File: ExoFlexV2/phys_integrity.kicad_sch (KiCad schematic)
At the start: 23 parts

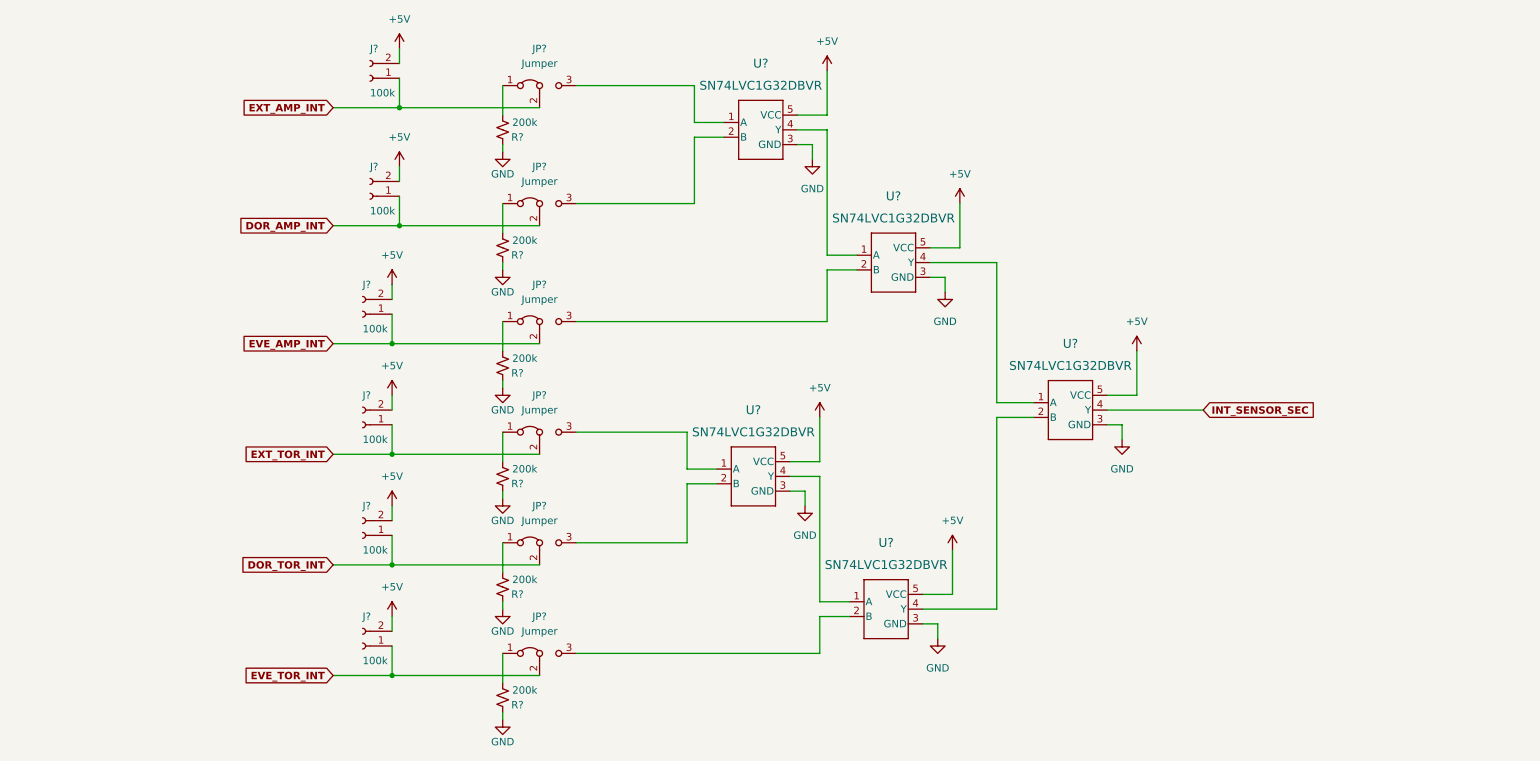
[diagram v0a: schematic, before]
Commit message: Mise à jour signaux STM
- Condo de découplage
- Signaux supplémentaire pour le STM
- Page GND sera pour Multiplexeur
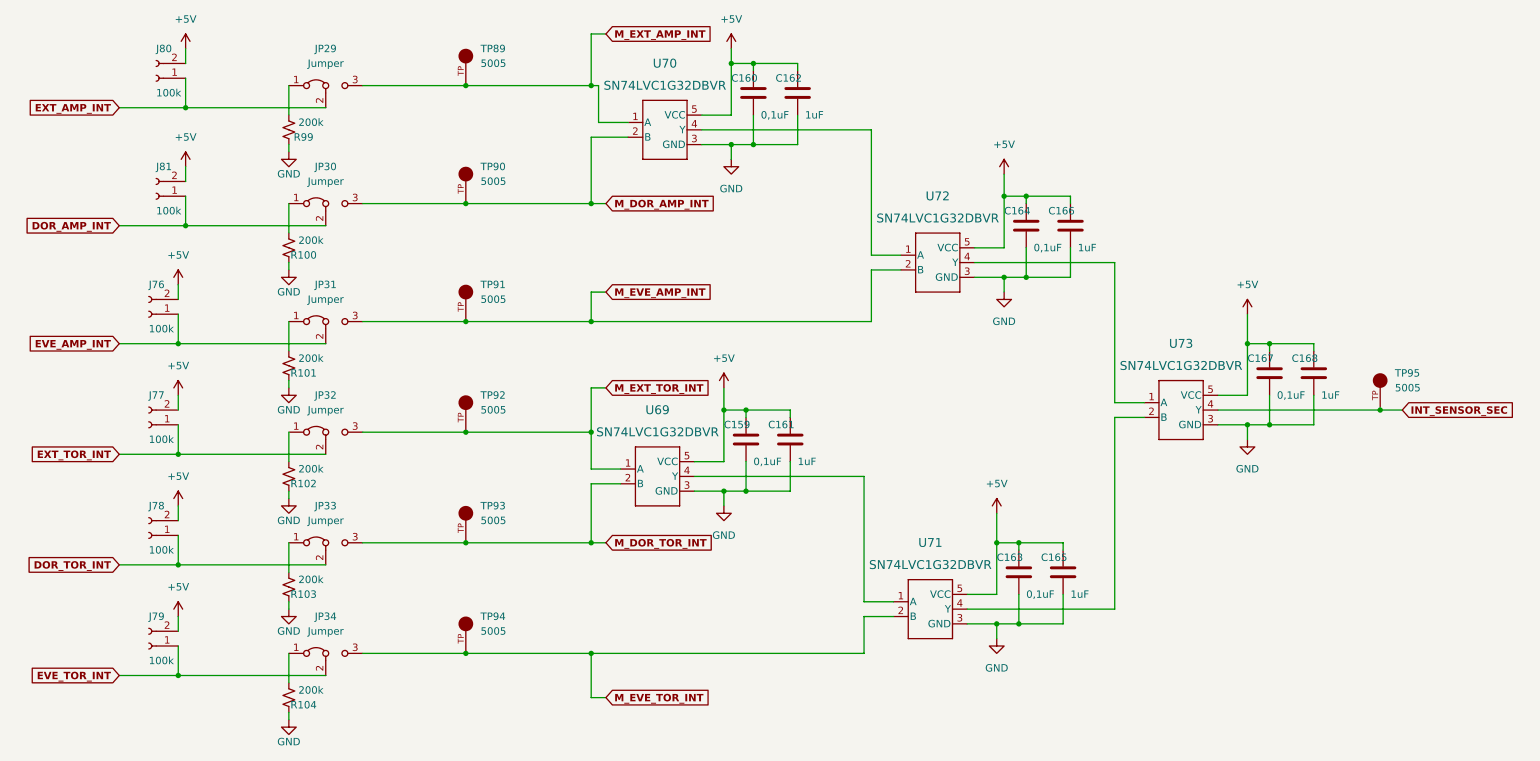
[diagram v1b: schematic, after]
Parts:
- added C159, C160, C163, C164, C167: 0,1uF, Capacitor_SMD:C_0603_1608Metric, symbol Device:C
- added C161, C162, C165, C166, C168: 1uF, Capacitor_SMD:C_0603_1608Metric, symbol Device:C
- added TP89, TP90, TP91, TP92, TP93, TP94, TP95: 5005, FootPrint:KEYSTONE_5005, symbol SymLib:5005
- gave numbers to parts that had none: 23
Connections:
- net +5V: now also C159.1, C160.1, C161.1, C162.1, C163.1, C164.1, C165.1, C166.1, C167.1, C168.1
- net GND: now also C159.2, C160.2, C161.2, C162.2, C163.2, C164.2, C165.2, C166.2, C167.2, C168.2
- net INT_SENSOR_SEC: now also TP95.TP
- net M_EXT_TOR_INT: now reaches JP32.3 (B), U69.1 (A)
- net M_EXT_TOR_INT: now also TP92.TP
- net M_DOR_TOR_INT: now reaches JP33.3 (B), U69.2 (B)
- net M_DOR_TOR_INT: now also TP93.TP
- net M_EXT_AMP_INT: now reaches JP29.3 (B), U70.1 (A)
- net M_EXT_AMP_INT: now also TP89.TP
- net M_DOR_AMP_INT: now reaches JP30.3 (B), U70.2 (B)
- net M_DOR_AMP_INT: now also TP90.TP
- net M_EVE_TOR_INT: now reaches JP34.3 (B), U71.2 (B)
- net M_EVE_TOR_INT: now also TP94.TP
- net M_EVE_AMP_INT: now reaches JP31.3 (B), U72.2 (B)
- net M_EVE_AMP_INT: now also TP91.TP
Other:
- moved on the sheet: J76, J77, J78, J79, J80, J81, JP29, JP30, JP31, JP32, JP33, JP34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

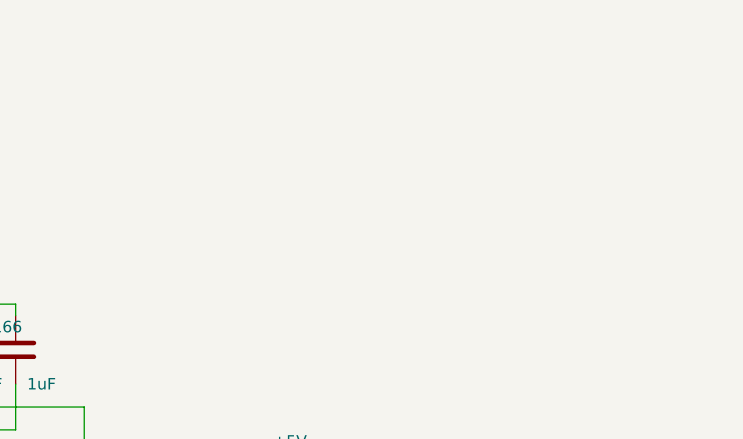
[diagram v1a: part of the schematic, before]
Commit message: Finalisation 1
- Ajout de pages pour la gestion des signaux négatif
- Modification des pages de torque et amplitude
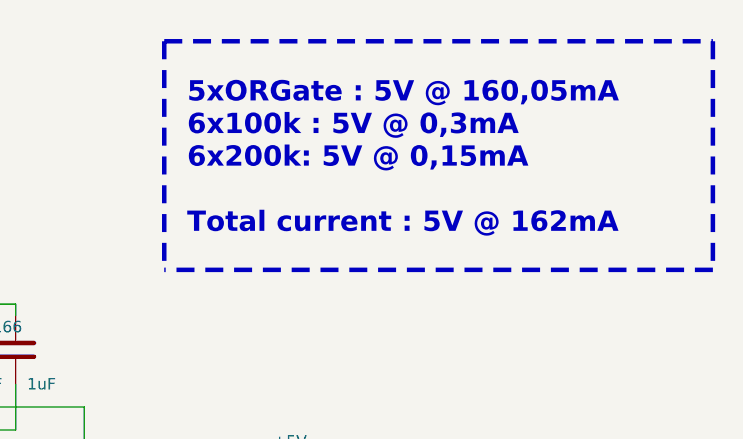
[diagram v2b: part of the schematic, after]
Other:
- note added: "5xORGate : 5V @ 160,05mA 6x100k : 5V @ 0,3mA 6x200k: 5V @ 0,15mA Total current : 5V @ 162mA"
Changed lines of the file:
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@@
     (stroke (width 0) (type default) (color 0 0 0 0))
+  )
+  (polyline (pts (xy 220.98 33.02) (xy 281.94 33.02))
+    (stroke (width 0.5) (type dash) (color 255 148 44 1))
   )
   (wire (pts (xy 50.8 106.68) (xy 76.2 106.68))
@@
     (stroke (width 0) (type default) (color 0 0 0 0))
   )
+  (polyline (pts (xy 281.94 33.02) (xy 281.94 58.42))
+    (stroke (width 0.5) (type dash) (color 255 148 44 1))
+  )
   (wire (pts (xy 168.91 140.97) (xy 168.91 134.62))
     (stroke (width 0) (type default) (color 0 0 0 0))
   )
+  (polyline (pts (xy 220.98 33.02) (xy 220.98 58.42))
+    (stroke (width 0.5) (type dash) (color 255 148 44 1))
+  )
   (wire (pts (xy 82.55 140.97) (xy 100.33 140.97))
     (stroke (width 0) (type default) (color 0 0 0 0))
@@
     (stroke (width 0) (type default) (color 0 0 0 0))
   )
+  (polyline (pts (xy 281.94 58.42) (xy 220.98 58.42))
+    (stroke (width 0.5) (type dash) (color 255 148 44 1))
+  )
   (wire (pts (xy 168.91 110.49) (xy 168.91 132.08))
     (stroke (width 0) (type default) (color 0 0 0 0))
@@
     (stroke (width 0) (type default) (color 0 0 0 0))
   )
+  (text "5xORGate : 5V @ 160,05mA\n6x100k : 5V @ 0,3mA\n6x200k: 5V @ 0,15mA\n\nTotal current : 5V @ 162mA"
+    (at 223.52 54.61 0)
+    (effects (font (size 2.25 2.25) (thickness 0.5) bold) (justify left bottom))
+  )
   (global_label "DOR_TOR_INT" (shape input) (at 40.64 125.73 180) (fields_autoplaced)
